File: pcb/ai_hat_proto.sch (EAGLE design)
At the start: 285 parts, among them J1 1X01-SM, J10 1X01-SM, J100 1X01-SM, J101 1X01-SM, J102 1X01-SM, J103 1X01-SM, J104 1X01-SM, J105 1X01-SM, J106 1X01-SM, J107 1X01-SM, J108 1X01-SM, J109 1X01-SM, J11 1X01-SM, J110 1X01-SM, J111 1X01-SM, J112 1X01-SM, J113 1X01-SM, J114 1X01-SM, J115 1X01-SM, J116 1X01-SM, J117 1X01-SM, J118 1X01-SM, J119 1X01-SM, J12 1X01-SM, J120 1X01-SM, J121 1X01-SM, J122 1X01-SM, J123 1X01-SM, J124 1X01-SM, J125 1X01-SM, J126 1X01-SM, J127 1X01-SM, J128 1X01-SM, J129 1X01-SM, J13 1X01-SM, J130 1X01-SM, J131 1X01-SM, J132 1X01-SM, J133 1X01-SM, J134 1X01-SM, J135 1X01-SM, J136 1X01-SM, J137 1X01-SM, J138 1X01-SM, J139 1X01-SM, J14 1X01-SM, J140 1X01-SM, J141 1X01-SM, J142 1X01-SM, J143 1X01-SM, J144 1X01-SM, J145 1X01-SM, J146 1X01-SM, J147 1X01-SM, J148 1X01-SM, J149 1X01-SM, J15 1X01-SM, J150 1X01-SM, J151 1X01-SM, J152 1X01-SM, J153 1X01-SM, J154 1X01-SM, J155 1X01-SM, J156 1X01-SM, J157 1X01-SM, J158 1X01-SM, J159 1X01-SM, J16 1X01-SM, J160 1X01-SM, J161 1X01-SM, J162 1X01-SM, J163 1X01-SM, J164 1X01-SM, J165 1X01-SM, J166 1X01-SM, J167 1X01-SM, J168 1X01-SM, J169 1X01-SM, J17 1X01-SM, J170 1X01-SM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

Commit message: updating
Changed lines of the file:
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@@
 <layer number="56" name="wert" color="7" fill="1" visible="no" active="no"/>
 <layer number="57" name="tCAD" color="7" fill="1" visible="no" active="no"/>
+<layer number="90" name="Modules" color="5" fill="1" visible="yes" active="yes"/>
 <layer number="91" name="Nets" color="2" fill="1" visible="yes" active="yes"/>
 <layer number="92" name="Busses" color="1" fill="1" visible="yes" active="yes"/>
@@
 <layer number="251" name="SMDround" color="7" fill="1" visible="yes" active="yes"/>
 <layer number="254" name="cooling" color="7" fill="1" visible="yes" active="yes"/>
+<layer number="255" name="routoute" color="7" fill="1" visible="yes" active="yes"/>
 </layers>
 <schematic xreflabel="%F%N/%S.%C%R" xrefpart="/%S.%C%R">

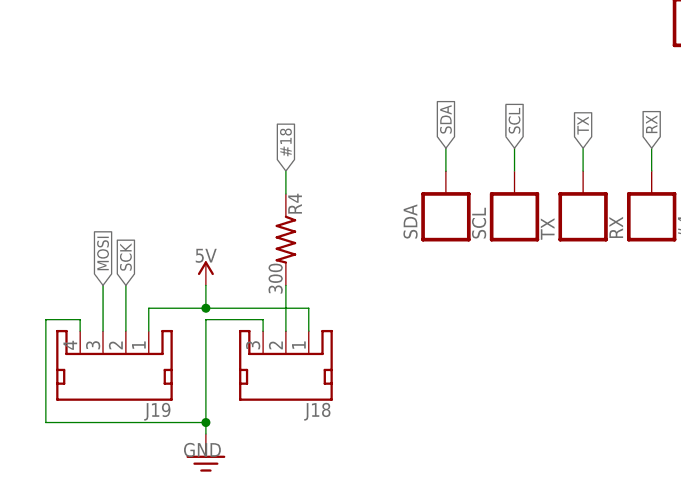
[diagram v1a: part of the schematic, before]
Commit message: changed resistor value
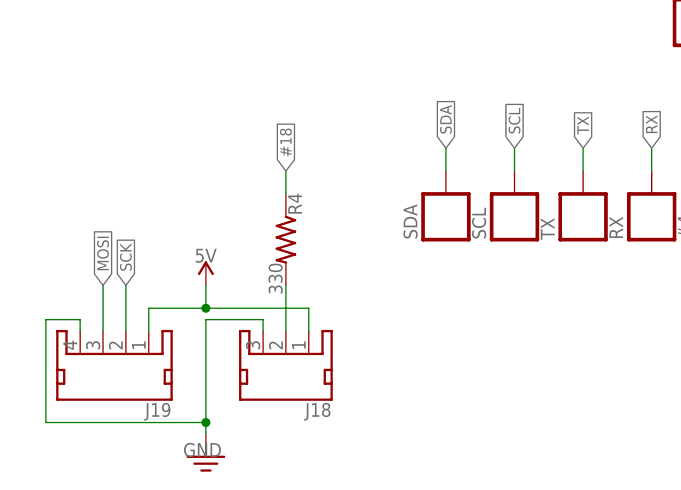
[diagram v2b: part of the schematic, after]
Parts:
- R4: value 300 -> 330
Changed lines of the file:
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@@
 <part name="J19" library="Ai_Connectors" deviceset="JST-4P-MALE" device=""/>
 <part name="GND7" library="Ai_Power" deviceset="GND" device=""/>
-<part name="R4" library="Ai_Passives" deviceset="RES" device="0603" value="300"/>
+<part name="R4" library="Ai_Passives" deviceset="RES" device="0603" value="330"/>
 <part name="FRAME1" library="Ai_Miscellany" deviceset="FRAME-LETTER" device="">
 <attribute name="AUTHOR" value="A.I. HARDWARE SITH LORDS"/>

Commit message: updating
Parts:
- added FRAME1: FRAME-LETTER, Ai_Miscellany:FRAME-LETTER
- C1: value 100nF -> 0.1uF
- R1, R2: value 3k9 -> 3K9
- R3: value 1k -> 1K
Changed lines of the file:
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@@
 <layer number="56" name="wert" color="7" fill="1" visible="no" active="no"/>
 <layer number="57" name="tCAD" color="7" fill="1" visible="no" active="no"/>
+<layer number="59" name="tCarbon" color="7" fill="1" visible="no" active="no"/>
+<layer number="60" name="bCarbon" color="7" fill="1" visible="no" active="no"/>
 <layer number="90" name="Modules" color="5" fill="1" visible="yes" active="yes"/>
 <layer number="91" name="Nets" color="2" fill="1" visible="yes" active="yes"/>
@@
 <layer number="112" name="tSilk" color="7" fill="1" visible="yes" active="yes"/>
 <layer number="113" name="Route13" color="7" fill="1" visible="no" active="no"/>
+<layer number="114" name="Badge_Outline" color="7" fill="1" visible="yes" active="yes"/>
+<layer number="115" name="ReferenceISLANDS" color="7" fill="1" visible="yes" active="yes"/>
 <layer number="116" name="Patch_BOT" color="7" fill="1" visible="yes" active="yes"/>
 <layer number="117" name="mPads" color="7" fill="1" visible="no" active="no"/>
@@
 <layer number="223" name="223bmp" color="24" fill="1" visible="no" active="no"/>
 <layer number="224" name="224bmp" color="25" fill="1" visible="no" active="no"/>
+<layer number="225" name="225bmp" color="7" fill="1" visible="no" active="yes"/>
+<layer number="226" name="226bmp" color="7" fill="1" visible="no" active="yes"/>
+<layer number="227" name="227bmp" color="7" fill="1" visible="no" active="yes"/>
+<layer number="228" name="228bmp" color="7" fill="1" visible="no" active="yes"/>
+<layer number="229" name="229bmp" color="7" fill="1" visible="yes" active="yes"/>
+<layer number="230" name="230bmp" color="7" fill="1" visible="no" active="yes"/>
+<layer number="231" name="231bmp" color="7" fill="1" visible="yes" active="yes"/>
 <layer number="248" name="Housing" color="7" fill="1" visible="yes" active="yes"/>
 <layer number="249" name="Edge" color="7" fill="1" visible="yes" active="yes"/>
@@
 <part name="U1" library="Ai_IC" deviceset="24LC32A" device=""/>
 <part name="GND10" library="Ai_Power" deviceset="GND" device=""/>
-<part name="R1" library="Ai_Passives" deviceset="RES" device="0603" value="3k9">
+<part name="R1" library="Ai_Passives" deviceset="RES" device="0603" value="3K9">
 <attribute name="TOLERANCE" value="5%"/>
 </part>
 <part name="GND1" library="Ai_Power" deviceset="GND" device=""/>
-<part name="C1" library="Ai_Passives" deviceset="CAP" device="0603" value="100nF">
+<part name="C1" library="Ai_Passives" deviceset="CAP" device="0603" value="0.1uF">
 <attribute name="DIELECTRIC" value="X7R"/>
 </part>
-<part name="R2" library="Ai_Passives" deviceset="RES" device="0603" value="3k9">
+<part name="R2" library="Ai_Passives" deviceset="RES" device="0603" value="3K9">
 <attribute name="TOLERANCE" value="5%"/>
 </part>
-<part name="R3" library="Ai_Passives" deviceset="RES" device="0603" value="1k">
+<part name="R3" library="Ai_Passives" deviceset="RES" device="0603" value="1K">
 <attribute name="TOLERANCE" value="5%"/>
 </part>
@@
 <part name="R4" library="Ai_Passives" deviceset="RES" device="0603" value="330"/>
 <part name="FRAME1" library="Ai_Miscellany" deviceset="FRAME-LETTER" device="">
-<attribute name="AUTHOR" value="A.I. HARDWARE SITH LORDS"/>
 <attribute name="REV" value="1.0"/>
 </part>
@@
 <instance part="R4" gate="G$1" x="31.75" y="29.21" rot="R270"/>
 <instance part="FRAME1" gate="G$1" x="0" y="0"/>
-<instance part="FRAME1" gate="G$2" x="147.32" y="0"/>
-<instance part="U$9" gate="G$1" x="139.7" y="16.51"/>
-<instance part="U$10" gate="G$1" x="139.7" y="16.51"/>
+<instance part="FRAME1" gate="G$2" x="154.94" y="3.81"/>
+<instance part="U$9" gate="G$1" x="147.32" y="19.05"/>
+<instance part="U$10" gate="G$1" x="147.32" y="19.05"/>
 <instance part="U$8" gate="G$1" x="22.86" y="24.13"/>
 </instances>
@@
 </schematic>
 </drawing>
+<compatibility>
+<note version="6.3" minversion="6.2.2" severity="warning">
+Since Version 6.2.2 text objects can contain more than one line,
+which will not be processed correctly with this version.
+</note>
+</compatibility>
 </eagle>
